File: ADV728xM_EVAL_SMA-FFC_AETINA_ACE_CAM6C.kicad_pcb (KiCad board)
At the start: 2 copper layers, 86.5 x 33.6 mm, 16 parts, among them J1 142-0701-801, J2 142-0701-801, J3 142-0701-801, J4 142-0701-801, J5 Conn_01x04_Male, J6 Conn_01x04_Male, J7 Conn_01x02_Male, J8 Conn_01x02_Male, J9 3-1734742-6, U1 NLSX5014DTR2G

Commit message: Add production release V1A with board outline
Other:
- board size 86.5 x 33.6 mm -> 86.5 x 33.7 mm
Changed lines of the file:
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@@
     )
   )
-  (gr_line (start 115.57 109.7534) (end 115.5827 76.1873) (layer Edge.Cuts) (width 0.05))
-  (gr_line (start 202.0189 109.8169) (end 115.697 109.728) (layer Edge.Cuts) (width 0.05))
+  (gr_line (start 115.5954 109.728) (end 115.5827 76.1619) (layer Edge.Cuts) (width 0.05))
+  (gr_line (start 202.0189 109.8169) (end 115.5954 109.728) (layer Edge.Cuts) (width 0.05))
   (gr_line (start 202.057 76.2254) (end 202.0189 109.8169) (layer Edge.Cuts) (width 0.05))
-  (gr_line (start 115.5827 76.1873) (end 201.93 76.2508) (layer Edge.Cuts) (width 0.05))
+  (gr_line (start 115.5827 76.1619) (end 202.057 76.2254) (layer Edge.Cuts) (width 0.05))
   (segment (start 152.2465 97.7403) (end 152.2349 97.7519) (width 0.35) (layer F.Cu) (net 1))
   (segment (start 154.1318 95.8007) (end 154.1272 95.7961) (width 0.25) (layer F.Cu) (net 1))
@@
     (polygon
       (pts
-        (xy 202.057 76.2127) (xy 202.0189 109.8169) (xy 115.7351 109.728) (xy 115.5954 76.1746)
+        (xy 202.057 76.2127) (xy 202.0189 109.8169) (xy 115.6081 109.728) (xy 115.5954 76.1746)
       )
     )
@@
     (polygon
       (pts
-        (xy 201.93 76.238033) (xy 201.8919 109.842233) (xy 115.6081 109.753333) (xy 115.57 76.187233)
+        (xy 202.057 76.2127) (xy 202.0189 109.8169) (xy 115.6081 109.753333) (xy 115.57 76.187233)
       )
     )

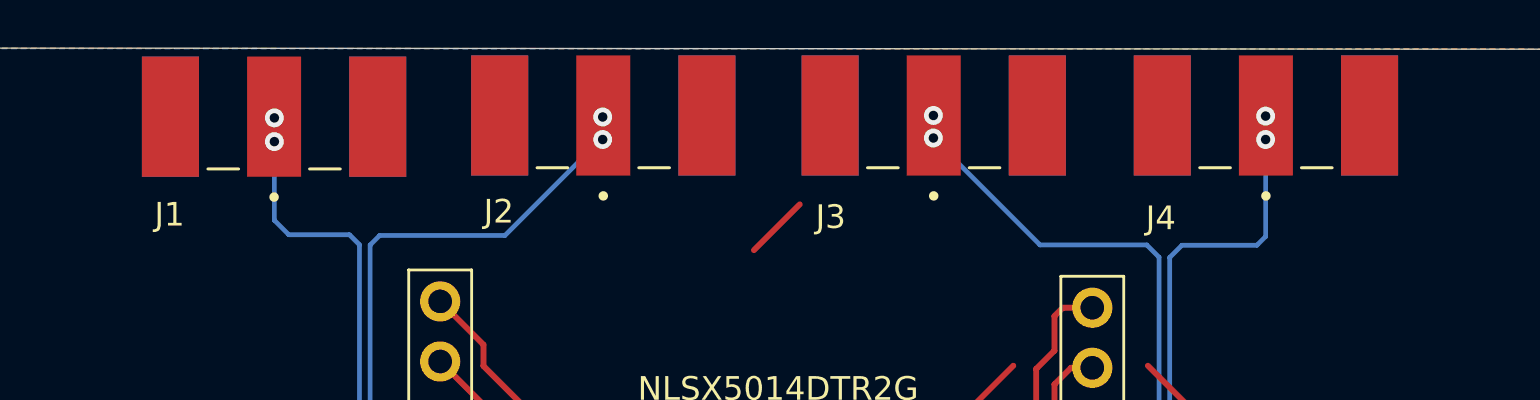
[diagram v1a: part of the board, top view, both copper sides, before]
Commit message: Move SMA connetors to back layer
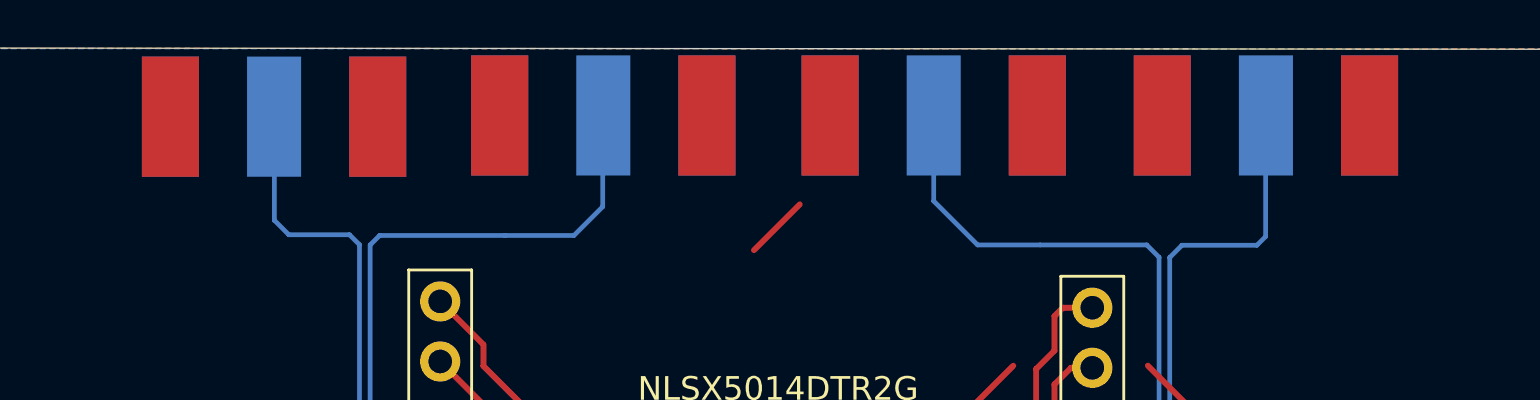
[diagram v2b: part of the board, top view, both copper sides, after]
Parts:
- J1, J2, J3, J4: moved to B.Cu
- turned J1 to 180 degrees
- turned J2 to 180 degrees
- turned J3 to 180 degrees
- turned J4 to 180 degrees
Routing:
- net /CLK_P: track 57.1 -> 59.6 mm, vias 3 -> 1
- net /D0_N: track 48.3 -> 49.9 mm, vias 3 -> 1
- net /D0_P: vias 3 -> 1
- net /CLK_N: vias 3 -> 1
